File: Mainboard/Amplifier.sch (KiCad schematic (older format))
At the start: 24 parts, among them U1 TAS5825M

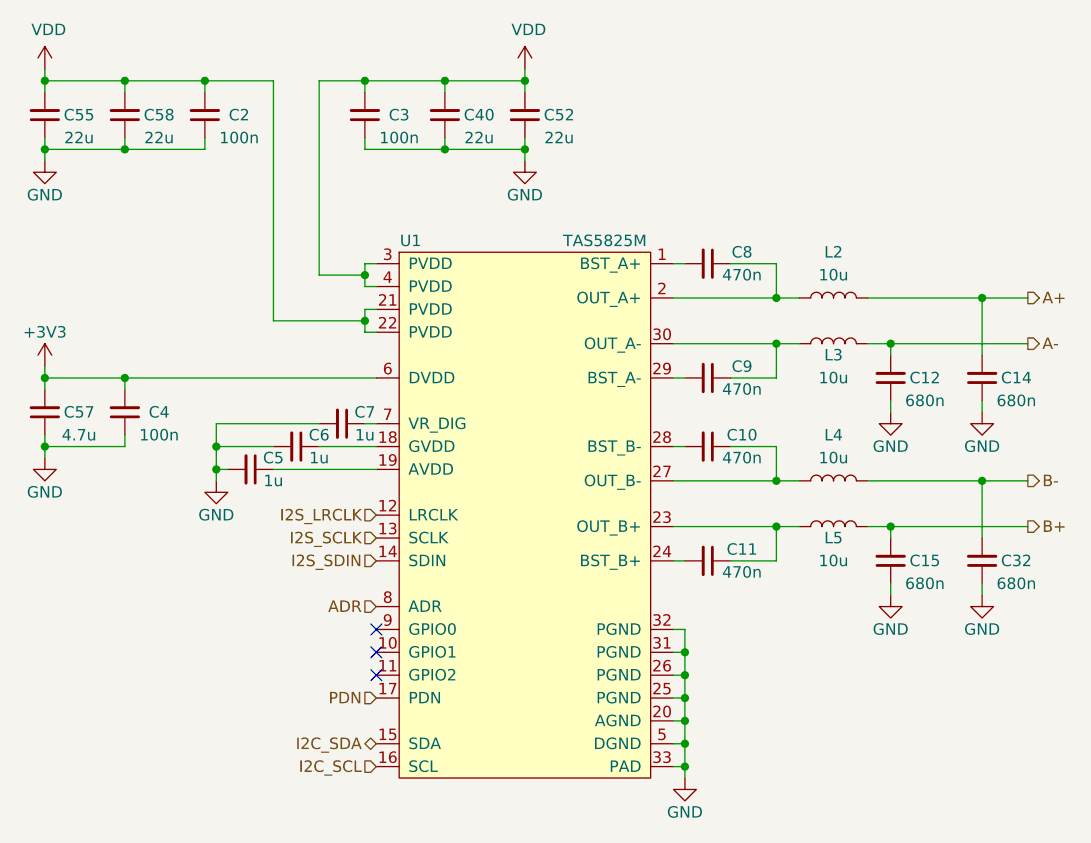
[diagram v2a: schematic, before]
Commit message: Clean up schematic for BoM export
- Change 22u 0805's (amp decoupling) to 15u
- Change 680n 0805's (part of output filter) to 470n
- Change C1 (amp bulk cap) from 820u to 1000u
- Add BoM.ini for KiBom export and
- Complete fields needed for KiBom (Manufacturer and partnumber)
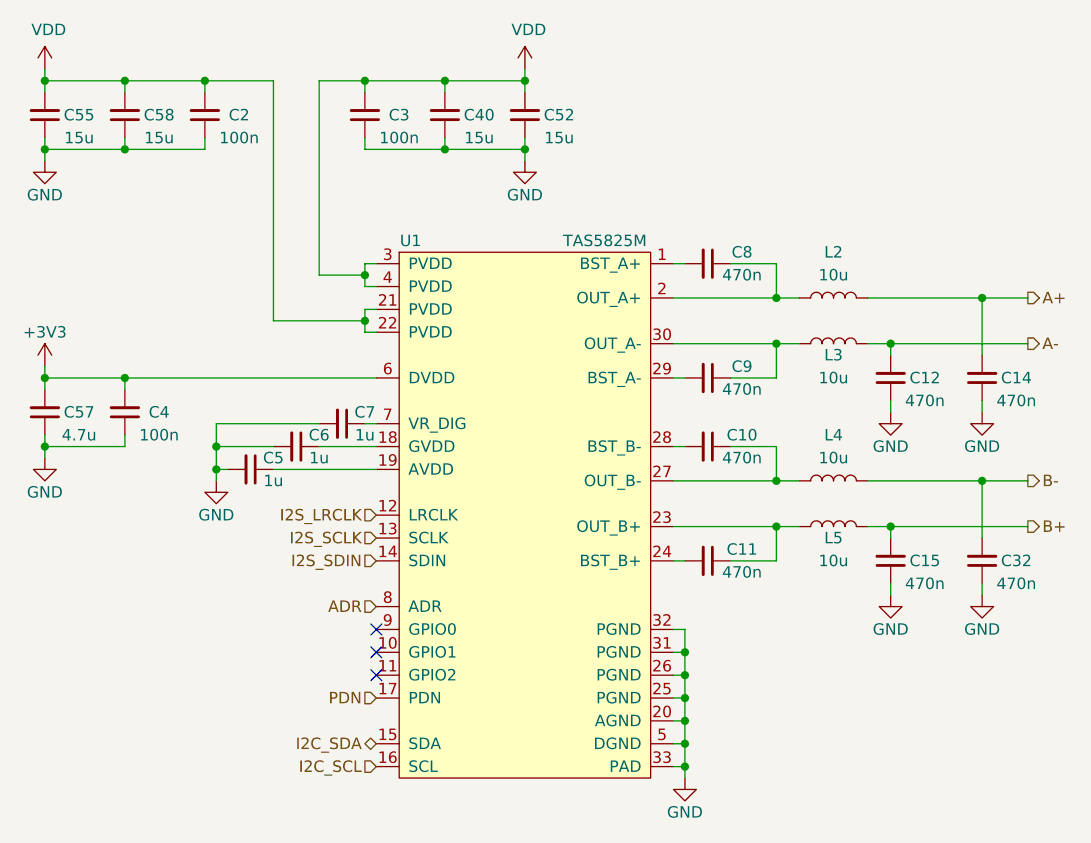
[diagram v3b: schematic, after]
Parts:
- C16, C30, C31, C33: value 680n -> 470n; Manufacturer (none) -> Kemet; Partnumber (none) -> C0805C474K5RACTU
- C19: Manufacturer (none) -> Samsung; Partnumber (none) -> CL21A475KPFNNNE
- C20, C24, C25: Manufacturer (none) -> Taiyo Yuden; Partnumber (none) -> UMK212B7105KG-T
- C26, C27, C28, C29: Manufacturer (none) -> Samsung; Partnumber (none) -> CL10B474KO8NFNC
- C41, C53, C56, C59: value 22u -> 15u; Manufacturer (none) -> TDK; Partnumber (none) -> C2012X5R1V156M125AC
- L6, L7, L8, L9: Manufacturer (none) -> Murata; Partnumber (none) -> 1274AS-H-100M=P3
- U1: Manufacturer (none) -> Texas Instruments; Partnumber (none) -> TAS5825M
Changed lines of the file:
@@
 AR Path="/60AAD6DF/61DB323F/61D73D33" Ref="C58"  Part="1"
 F 0 "C58" H 3800 2450 50  0000 C CNN
-F 1 "22u" H 3800 2550 50  0000 C CNN
+F 1 "15u" H 3800 2550 50  0000 C CNN
 F 2 "Capacitor_SMD:C_0805_2012Metric" H 3950 2450 50  0001 C CNN
 F 3 "~" H 3950 2450 50  0001 C CNN
+F 4 "TDK" H 3950 2450 50  0001 C CNN "Manufacturer"
+F 5 "C2012X5R1V156M125AC" H 3950 2450 50  0001 C CNN "Partnumber"
 	1    3950 2450
 	-1   0    0    1
@@
 AR Path="/60AAD6DF/61DB323F/61D73D2D" Ref="C55"  Part="1"
 F 0 "C55" H 3450 2450 50  0000 C CNN
-F 1 "22u" H 3450 2550 50  0000 C CNN
+F 1 "15u" H 3450 2550 50  0000 C CNN
 F 2 "Capacitor_SMD:C_0805_2012Metric" H 3600 2450 50  0001 C CNN
 F 3 "~" H 3600 2450 50  0001 C CNN
+F 4 "TDK" H 3600 2450 50  0001 C CNN "Manufacturer"
+F 5 "C2012X5R1V156M125AC" H 3600 2450 50  0001 C CNN "Partnumber"
 	1    3600 2450
 	-1   0    0    1
@@
 F 2 "Capacitor_SMD:C_0805_2012Metric" H 3600 3750 50  0001 C CNN
 F 3 "~" H 3600 3750 50  0001 C CNN
+F 4 "Samsung" H 3600 3750 50  0001 C CNN "Manufacturer"
+F 5 "CL21A475KPFNNNE" H 3600 3750 50  0001 C CNN "Partnumber"
 	1    3600 3750
 	-1   0    0    1
@@
 AR Path="/60AAD6DF/61DB323F/61D73CE8" Ref="C52"  Part="1"
 F 0 "C52" H 5550 2450 50  0000 C CNN
-F 1 "22u" H 5550 2550 50  0000 C CNN
+F 1 "15u" H 5550 2550 50  0000 C CNN
 F 2 "Capacitor_SMD:C_0805_2012Metric" H 5700 2450 50  0001 C CNN
 F 3 "~" H 5700 2450 50  0001 C CNN
+F 4 "TDK" H 5700 2450 50  0001 C CNN "Manufacturer"
+F 5 "C2012X5R1V156M125AC" H 5700 2450 50  0001 C CNN "Partnumber"
 	1    5700 2450
 	-1   0    0    1
@@
 AR Path="/60AAD6DF/61DB323F/61D73CE2" Ref="C40"  Part="1"
 F 0 "C40" H 5200 2450 50  0000 C CNN
-F 1 "22u" H 5200 2550 50  0000 C CNN
+F 1 "15u" H 5200 2550 50  0000 C CNN
 F 2 "Capacitor_SMD:C_0805_2012Metric" H 5350 2450 50  0001 C CNN
 F 3 "~" H 5350 2450 50  0001 C CNN
+F 4 "TDK" H 5350 2450 50  0001 C CNN "Manufacturer"
+F 5 "C2012X5R1V156M125AC" H 5350 2450 50  0001 C CNN "Partnumber"
 	1    5350 2450
 	-1   0    0    1
@@
 F 2 "ZOUDIO-footprints:TAS5825M" H 5700 4300 50  0001 C CNN
 F 3 "" H 5700 4300 50  0001 C CNN
+F 4 "Texas Instruments" H 5700 4200 50  0001 C CNN "Manufacturer"
+F 5 "TAS5825M" H 5700 4200 50  0001 C CNN "Partnumber"
 	1    5700 4200
 	1    0    0    -1
@@
 AR Path="/60AAD6DF/61DB323F/61D73CA4" Ref="C32"  Part="1"
 F 0 "C32" H 7550 4400 50  0000 C CNN
-F 1 "680n" H 7550 4500 50  0000 C CNN
+F 1 "470n" H 7550 4500 50  0000 C CNN
 F 2 "Capacitor_SMD:C_0805_2012Metric" H 7700 4400 50  0001 C CNN
 F 3 "~" H 7700 4400 50  0001 C CNN
+F 4 "Kemet" H 7700 4400 50  0001 C CNN "Manufacturer"
+F 5 "C0805C474K5RACTU" H 7700 4400 50  0001 C CNN "Partnumber"
 	1    7700 4400
 	-1   0    0    1
@@
 F 2 "Capacitor_SMD:C_0603_1608Metric" H 6500 3100 50  0001 C CNN
 F 3 "~" H 6500 3100 50  0001 C CNN
+F 4 "Samsung" H 6500 3100 50  0001 C CNN "Manufacturer"
+F 5 "CL10B474KO8NFNC" H 6500 3100 50  0001 C CNN "Partnumber"
 	1    6500 3100
 	0    1    1    0
@@
 F 2 "Capacitor_SMD:C_0603_1608Metric" H 6500 3600 50  0001 C CNN
 F 3 "~" H 6500 3600 50  0001 C CNN
+F 4 "Samsung" H 6500 3600 50  0001 C CNN "Manufacturer"
+F 5 "CL10B474KO8NFNC" H 6500 3600 50  0001 C CNN "Partnumber"
 	1    6500 3600
 	0    1    1    0
@@
 F 2 "Capacitor_SMD:C_0603_1608Metric" H 6500 3900 50  0001 C CNN
 F 3 "~" H 6500 3900 50  0001 C CNN
+F 4 "Samsung" H 6500 3900 50  0001 C CNN "Manufacturer"
+F 5 "CL10B474KO8NFNC" H 6500 3900 50  0001 C CNN "Partnumber"
 	1    6500 3900
 	0    1    1    0
@@
 F 2 "Capacitor_SMD:C_0603_1608Metric" H 6500 4400 50  0001 C CNN
 F 3 "~" H 6500 4400 50  0001 C CNN
+F 4 "Samsung" H 6500 4400 50  0001 C CNN "Manufacturer"
+F 5 "CL10B474KO8NFNC" H 6500 4400 50  0001 C CNN "Partnumber"
 	1    6500 4400
 	0    1    1    0
@@
 AR Path="/60AAD6DF/61DB323F/61D73C56" Ref="C12"  Part="1"
 F 0 "C12" H 7150 3600 50  0000 C CNN
-F 1 "680n" H 7150 3700 50  0000 C CNN
+F 1 "470n" H 7150 3700 50  0000 C CNN
 F 2 "Capacitor_SMD:C_0805_2012Metric" H 7300 3600 50  0001 C CNN
 F 3 "~" H 7300 3600 50  0001 C CNN
+F 4 "Kemet" H 7300 3600 50  0001 C CNN "Manufacturer"
+F 5 "C0805C474K5RACTU" H 7300 3600 50  0001 C CNN "Partnumber"
 	1    7300 3600
 	-1   0    0    1
@@
 AR Path="/60AAD6DF/61DB323F/61D73C5C" Ref="C14"  Part="1"
 F 0 "C14" H 7550 3600 50  0000 C CNN
-F 1 "680n" H 7550 3700 50  0000 C CNN
+F 1 "470n" H 7550 3700 50  0000 C CNN
 F 2 "Capacitor_SMD:C_0805_2012Metric" H 7700 3600 50  0001 C CNN
 F 3 "~" H 7700 3600 50  0001 C CNN
+F 4 "Kemet" H 7700 3600 50  0001 C CNN "Manufacturer"
+F 5 "C0805C474K5RACTU" H 7700 3600 50  0001 C CNN "Partnumber"
 	1    7700 3600
 	-1   0    0    1
@@
 F 2 "ZOUDIO-footprints:Murata_1274AS-H-100M" H 7050 4050 50  0001 C CNN
 F 3 "~" H 7050 4050 50  0001 C CNN
+F 4 "Murata" H 7050 4050 50  0001 C CNN "Manufacturer"
+F 5 "1274AS-H-100M=P3" H 7050 4050 50  0001 C CNN "Partnumber"
 	1    7050 4050
 	0    -1   -1   0
@@
 F 2 "ZOUDIO-footprints:Murata_1274AS-H-100M" H 7050 4250 50  0001 C CNN
 F 3 "~" H 7050 4250 50  0001 C CNN
+F 4 "Murata" H 7050 4250 50  0001 C CNN "Manufacturer"
+F 5 "1274AS-H-100M=P3" H 7050 4250 50  0001 C CNN "Partnumber"
 	1    7050 4250
 	0    -1   -1   0
@@
 F 2 "ZOUDIO-footprints:Murata_1274AS-H-100M" H 7050 3450 50  0001 C CNN
 F 3 "~" H 7050 3450 50  0001 C CNN
+F 4 "Murata" H 7050 3450 50  0001 C CNN "Manufacturer"
+F 5 "1274AS-H-100M=P3" H 7050 3450 50  0001 C CNN "Partnumber"
 	1    7050 3450
 	0    -1   -1   0
@@
 F 2 "ZOUDIO-footprints:Murata_1274AS-H-100M" H 7050 3250 50  0001 C CNN
 F 3 "~" H 7050 3250 50  0001 C CNN
+F 4 "Murata" H 7050 3250 50  0001 C CNN "Manufacturer"
+F 5 "1274AS-H-100M=P3" H 7050 3250 50  0001 C CNN "Partnumber"
 	1    7050 3250
 	0    -1   -1   0
@@
 AR Path="/60AAD6DF/61DB323F/61D73C9E" Ref="C15"  Part="1"
 F 0 "C15" H 7150 4400 50  0000 C CNN
-F 1 "680n" H 7150 4500 50  0000 C CNN
+F 1 "470n" H 7150 4500 50  0000 C CNN
 F 2 "Capacitor_SMD:C_0805_2012Metric" H 7300 4400 50  0001 C CNN
 F 3 "~" H 7300 4400 50  0001 C CNN
+F 4 "Kemet" H 7300 4400 50  0001 C CNN "Manufacturer"
+F 5 "C0805C474K5RACTU" H 7300 4400 50  0001 C CNN "Partnumber"
 	1    7300 4400
 	-1   0    0    1
@@
 F 2 "Capacitor_SMD:C_0805_2012Metric" H 4900 3800 50  0001 C CNN
 F 3 "~" H 4900 3800 50  0001 C CNN
+F 4 "Taiyo Yuden" H 4900 3800 50  0001 C CNN "Manufacturer"
+F 5 "UMK212B7105KG-T" H 4900 3800 50  0001 C CNN "Partnumber"
 	1    4900 3800
 	0    1    1    0
@@
 F 2 "Capacitor_SMD:C_0805_2012Metric" H 4700 3900 50  0001 C CNN
 F 3 "~" H 4700 3900 50  0001 C CNN
+F 4 "Taiyo Yuden" H 4700 3900 50  0001 C CNN "Manufacturer"
+F 5 "UMK212B7105KG-T" H 4700 3900 50  0001 C CNN "Partnumber"
 	1    4700 3900
 	0    1    1    0
@@
 F 2 "Capacitor_SMD:C_0805_2012Metric" H 4500 4000 50  0001 C CNN
 F 3 "~" H 4500 4000 50  0001 C CNN
+F 4 "Taiyo Yuden" H 4500 4000 50  0001 C CNN "Manufacturer"
+F 5 "UMK212B7105KG-T" H 4500 4000 50  0001 C CNN "Partnumber"
 	1    4500 4000
 	0    1    1    0
